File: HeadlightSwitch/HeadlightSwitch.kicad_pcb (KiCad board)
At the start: 2 copper layers, 88.4 x 25.4 mm, 24 parts, among them J0 Battery-, J101 Battery+, J102 MarkerTail+, J103 Headlight+, J104 Headlight-, Q101 BCX56, SW101 SW_Rotary3x4, U101 LM555xM

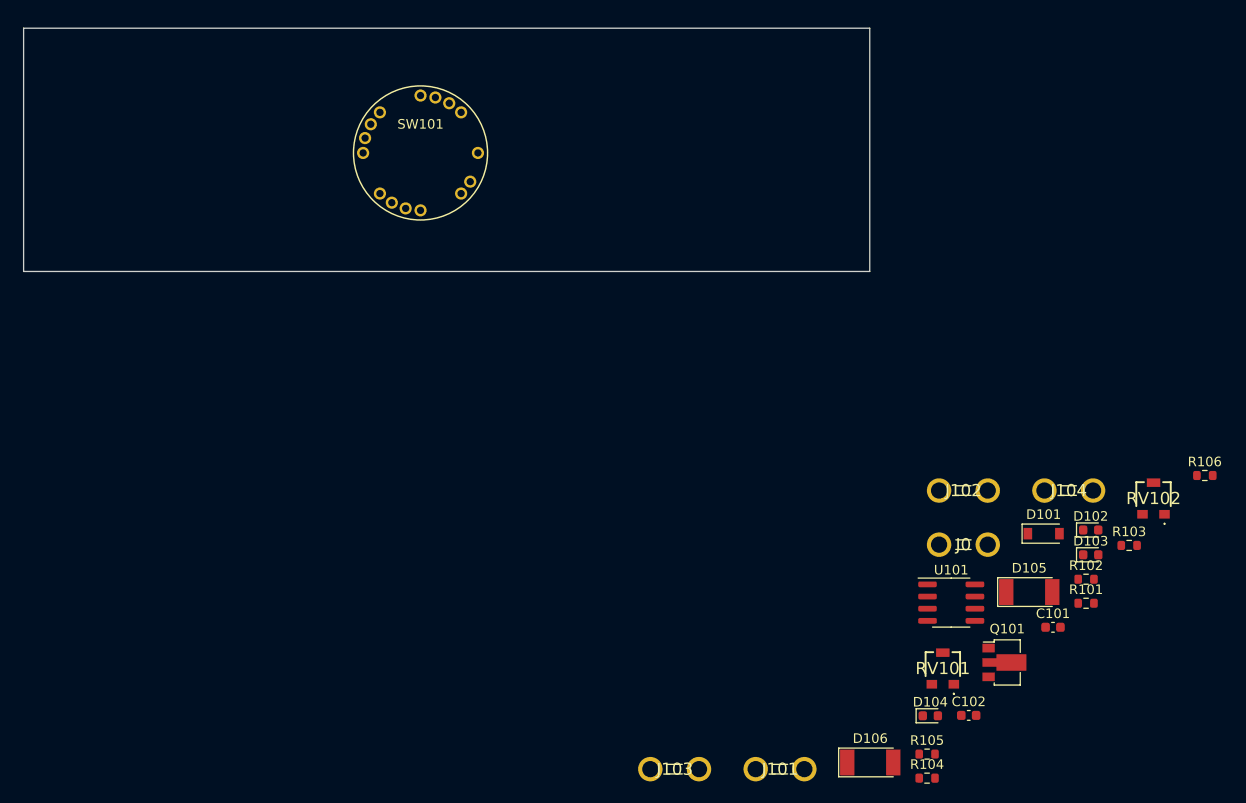
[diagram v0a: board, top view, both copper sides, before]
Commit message: Complete Headlight Switch Board.
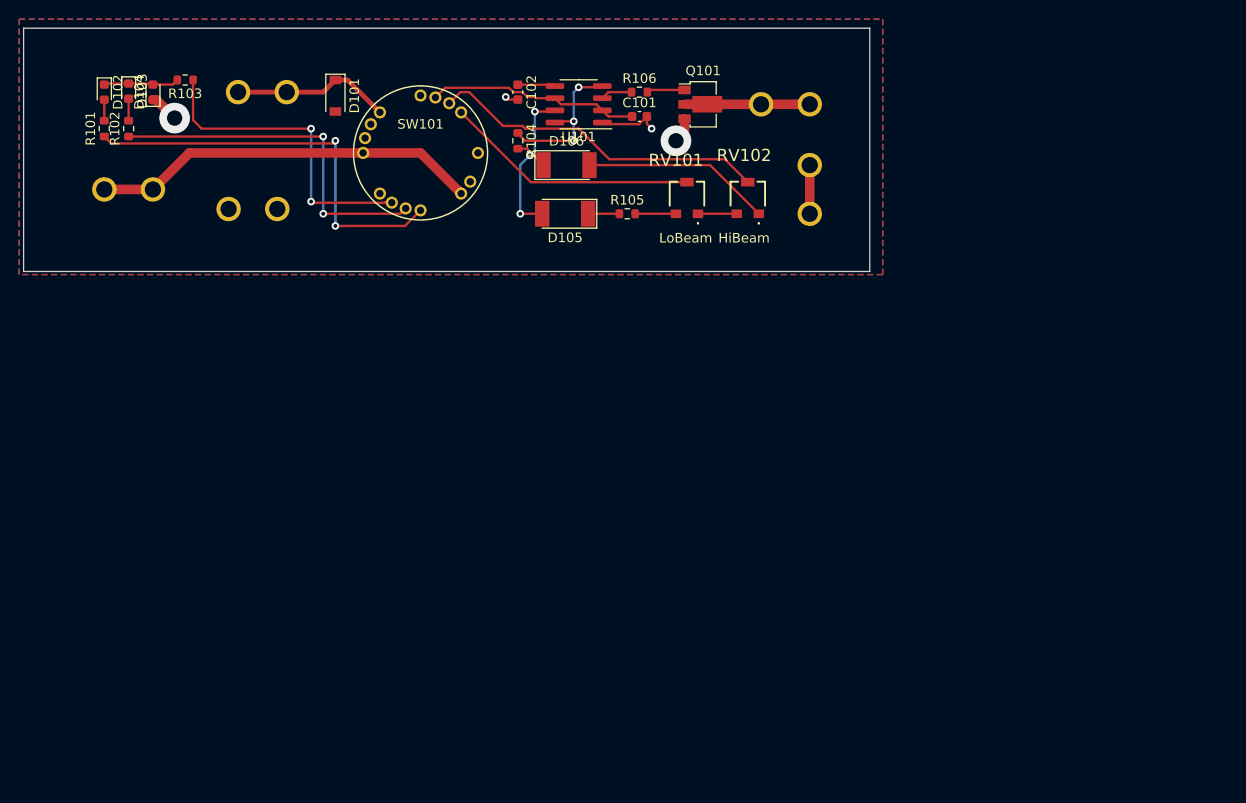
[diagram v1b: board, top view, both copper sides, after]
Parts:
- J0, J101, J102, J103, J104: moved to B.Cu
- moved R101 113.9 mm to (95.2, 67.3), turned to 90 degrees
- moved D102 112.7 mm to (95.2, 63.5), turned to -90 degrees
- moved D103 111.5 mm to (97.8, 63.4), turned to -90 degrees
- moved R102 110.5 mm to (97.8, 67.3), turned to 90 degrees
- moved R103 109.9 mm to (103.7, 62.2), turned to 180 degrees
- moved D104 104.1 mm to (100.3, 63.5), turned to 90 degrees
- moved J101 91.0 mm to (95.2, 73.7)
- moved D101 86.9 mm to (119.4, 63.9), turned to -90 degrees
- moved C102 80.3 mm to (138.4, 63.5), turned to -90 degrees
- moved J102 79.8 mm to (114.3, 63.5), turned to 180 degrees
- moved R104 79.1 mm to (138.4, 68.6), turned to -90 degrees
- moved J0 77.5 mm to (113.3, 75.7), turned to 180 degrees
- moved R106 71.3 mm to (151.1, 63.5)
- moved D106 70.0 mm to (143.5, 71.1)
- moved C101 68.6 mm to (151.1, 66.0)
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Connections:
- net Net-(D101-Pad1) renamed /MarkerTail+
- net Net-(J104-Pad1) renamed /Headlight-
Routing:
- net Net-(R101-Pad1): track 0.00 -> 43.0 mm, vias 0 -> 2
- net +12V: track 0.00 -> 40.6 mm
- net Net-(R102-Pad1): track 0.00 -> 37.2 mm, vias 0 -> 2
- net /PWHigh: track 0.00 -> 35.5 mm
- net Net-(R103-Pad1): track 0.00 -> 33.0 mm, vias 0 -> 2
- net /PWLow: track 0.00 -> 26.6 mm
- net /PWCommon: track 0.00 -> 22.2 mm
- net /HLightPower: track 0.00 -> 22.1 mm, vias 0 -> 3
- net Net-(D105-Pad2): track 0.00 -> 21.3 mm, vias 0 -> 3
- net Net-(D106-Pad2): track 0.00 -> 19.8 mm
- net /MarkerTail+: track 0.00 -> 16.7 mm
- net GNDPWR: track 0.00 -> 13.6 mm, vias 0 -> 4
- net /Headlight-: track 0.00 -> 13.0 mm
- net Net-(D102-Pad1): track 0.00 -> 7.91 mm
- net Net-(R105-Pad2): track 0.00 -> 4.25 mm
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- added copper zone on F.Cu, net /HLightPower
- added copper zone on B.Cu, net GNDPWR
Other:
- board text added: "HiBeam"
- board text added: "LoBeam"

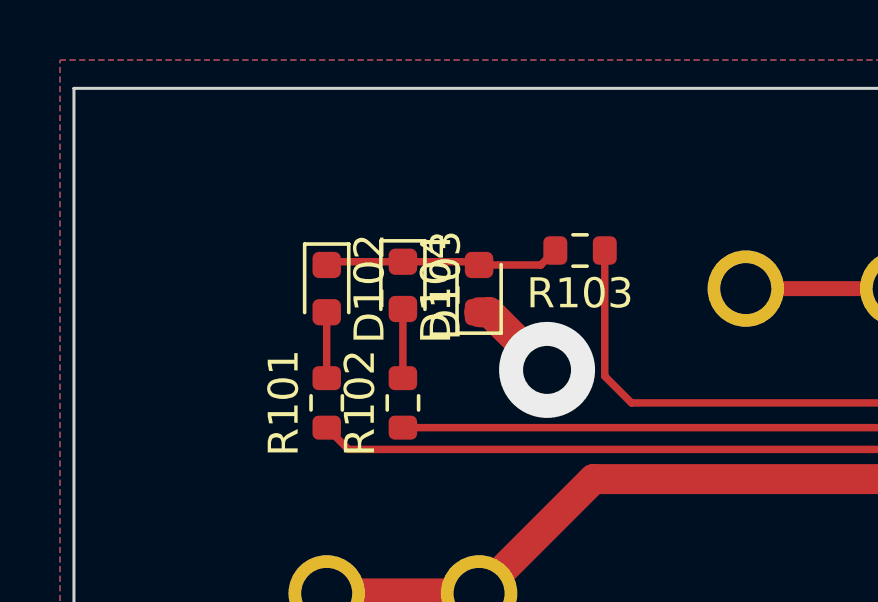
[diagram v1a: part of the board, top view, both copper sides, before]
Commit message: Add dims.
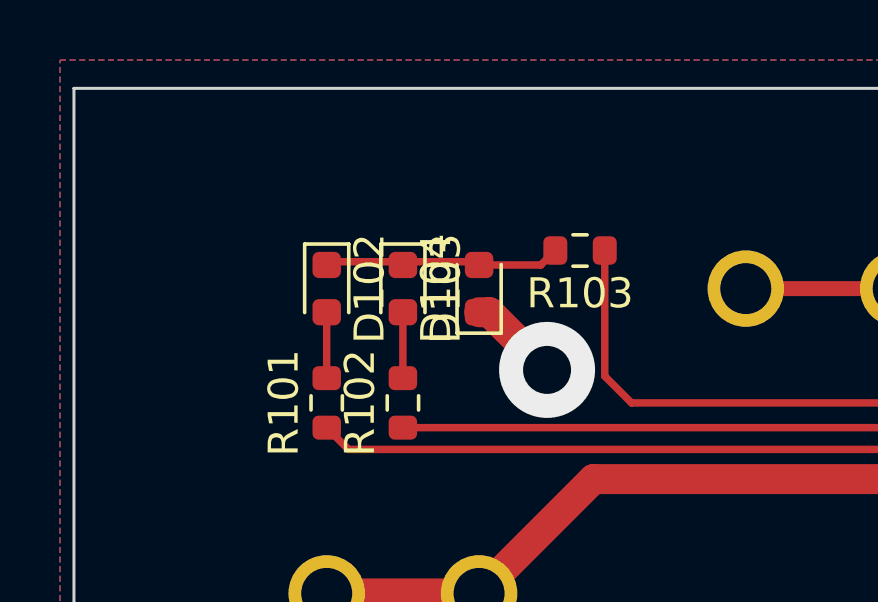
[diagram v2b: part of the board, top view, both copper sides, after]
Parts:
- moved D103 0.11 mm to (97.8, 63.5)
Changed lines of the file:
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@@
   )
   (footprint "LED_SMD:LED_0603_1608Metric" (layer "F.Cu")
-    (at 97.79 63.3925 -90)
+    (at 97.79 63.5 -90)
     (descr "LED SMD 0603 (1608 Metric), square (rectangular) end terminal, IPC_7351 nominal, (Body size source: http://www.tortai-tech.com/upload/download/2011102023233369053.pdf), generated with kicad-footprint-generator")
     (tags "LED")
@@
     )
   )
+  (gr_line (start 100.33 63.5) (end 86.868 63.5) (layer "Dwgs.User") (width 0.15))
   (gr_rect (start 90 60) (end 172 79.05) (layer "Dwgs.User") (width 0.2) (fill none))
   (gr_rect (start 86.825 56.825) (end 175.175 82.225) (layer "Edge.Cuts") (width 0.1) (fill none))
@@
     (effects (font (size 1 1) (thickness 0.15)))
   )
+  (dimension (type aligned) (layer "Dwgs.User")
+    (pts (xy 175.175 82.225) (xy 175.175 56.825))
+    (height 11.261)
+    (gr_text "25.4000 mm" (at 185.286 69.525 90) (layer "Dwgs.User")
+      (effects (font (size 1 1) (thickness 0.15)))
+    )
+    (format (units 3) (units_format 1) (precision 4))
+    (style (thickness 0.15) (arrow_length 1.27) (text_position_mode 0) (extension_height 0.58642) (extension_offset 0.5) keep_text_aligned)
+  )
+  (dimension (type aligned) (layer "Dwgs.User")
+    (pts (xy 172 60) (xy 90 60))
+    (height 7.93)
+    (gr_text "82.0000 mm" (at 131 50.92) (layer "Dwgs.User")
+      (effects (font (size 1 1) (thickness 0.15)))
+    )
+    (format (units 3) (units_format 1) (precision 4))
+    (style (thickness 0.15) (arrow_length 1.27) (text_position_mode 0) (extension_height 0.58642) (extension_offset 0.5) keep_text_aligned)
+  )
+  (dimension (type aligned) (layer "Dwgs.User")
+    (pts (xy 95.25 63.5) (xy 95.25 56.896))
+    (height -10.414)
+    (gr_text "6.6040 mm" (at 83.686 60.198 90) (layer "Dwgs.User")
+      (effects (font (size 1 1) (thickness 0.15)))
+    )
+    (format (units 3) (units_format 1) (precision 4))
+    (style (thickness 0.15) (arrow_length 1.27) (text_position_mode 0) (extension_height 0.58642) (extension_offset 0.5) keep_text_aligned)
+  )
+  (dimension (type aligned) (layer "Dwgs.User")
+    (pts (xy 97.79 63.5) (xy 95.25 63.5))
+    (height 13.208)
+    (gr_text "2.5400 mm" (at 96.52 49.142) (layer "Dwgs.User")
+      (effects (font (size 1 1) (thickness 0.15)))
+    )
+    (format (units 3) (units_format 1) (precision 4))
+    (style (thickness 0.15) (arrow_length 1.27) (text_position_mode 0) (extension_height 0.58642) (extension_offset 0.5) keep_text_aligned)
+  )
+  (dimension (type aligned) (layer "Dwgs.User")
+    (pts (xy 100.33 63.5) (xy 97.79 63.5))
+    (height 15.747999)
+    (gr_text "2.5400 mm" (at 99.06 46.602001) (layer "Dwgs.User")
+      (effects (font (size 1 1) (thickness 0.15)))
+    )
+    (format (units 3) (units_format 1) (precision 4))
+    (style (thickness 0.15) (arrow_length 1.27) (text_position_mode 0) (extension_height 0.58642) (extension_offset 0.5) keep_text_aligned)
+  )
+  (dimension (type aligned) (layer "Dwgs.User")
+    (pts (xy 86.825 56.825) (xy 175.175 56.825))
+    (height -13.391)
+    (gr_text "88.3500 mm" (at 131 42.284) (layer "Dwgs.User")
+      (effects (font (size 1 1) (thickness 0.15)))
+    )
+    (format (units 3) (units_format 1) (precision 4))
+    (style (thickness 0.15) (arrow_length 1.27) (text_position_mode 0) (extension_height 0.58642) (extension_offset 0.5) keep_text_aligned)
+  )
+  (dimension (type aligned) (layer "Dwgs.User")
+    (pts (xy 95.25 63.5) (xy 86.868 63.5))
+    (height 8.635999)
+    (gr_text "8.3820 mm" (at 91.059 53.714001) (layer "Dwgs.User")
+      (effects (font (size 1 1) (thickness 0.15)))
+    )
+    (format (units 3) (units_format 1) (precision 4))
+    (style (thickness 0.15) (arrow_length 1.27) (text_position_mode 0) (extension_height 0.58642) (extension_offset 0.5) keep_text_aligned)
+  )
+  (dimension (type aligned) (layer "Dwgs.User")
+    (pts (xy 128.27 69.85) (xy 86.825 69.85))
+    (height -15.748)
+    (gr_text "41.4450 mm" (at 107.5475 84.448) (layer "Dwgs.User")
+      (effects (font (size 1 1) (thickness 0.15)))
+    )
+    (format (units 3) (units_format 1) (precision 4))
+    (style (thickness 0.15) (arrow_length 1.27) (text_position_mode 0) (extension_height 0.58642) (extension_offset 0.5) keep_text_aligned)
+  )
+  (dimension (type aligned) (layer "Dwgs.User")
+    (pts (xy 172 60) (xy 172 79.05))
+    (height -8.34)
+    (gr_text "19.0500 mm" (at 179.19 69.525 90) (layer "Dwgs.User")
+      (effects (font (size 1 1) (thickness 0.15)))
+    )
+    (format (units 3) (units_format 1) (precision 4))
+    (style (thickness 0.15) (arrow_length 1.27) (text_position_mode 0) (extension_height 0.58642) (extension_offset 0.5) keep_text_aligned)
+  )
+  (dimension (type aligned) (layer "Dwgs.User")
+    (pts (xy 128.27 69.85) (xy 128.27 56.896))
+    (height -45.974)
+    (gr_text "12.9540 mm" (at 81.146 63.373 90) (layer "Dwgs.User")
+      (effects (font (size 1 1) (thickness 0.15)))
+    )
+    (format (units 3) (units_format 1) (precision 4))
+    (style (thickness 0.15) (arrow_length 1.27) (text_position_mode 0) (extension_height 0.58642) (extension_offset 0.5) keep_text_aligned)
+  )
   (segment (start 139.415817 64.008) (end 138.907817 63.5) (width 0.25) (layer "F.Cu") (net 1))

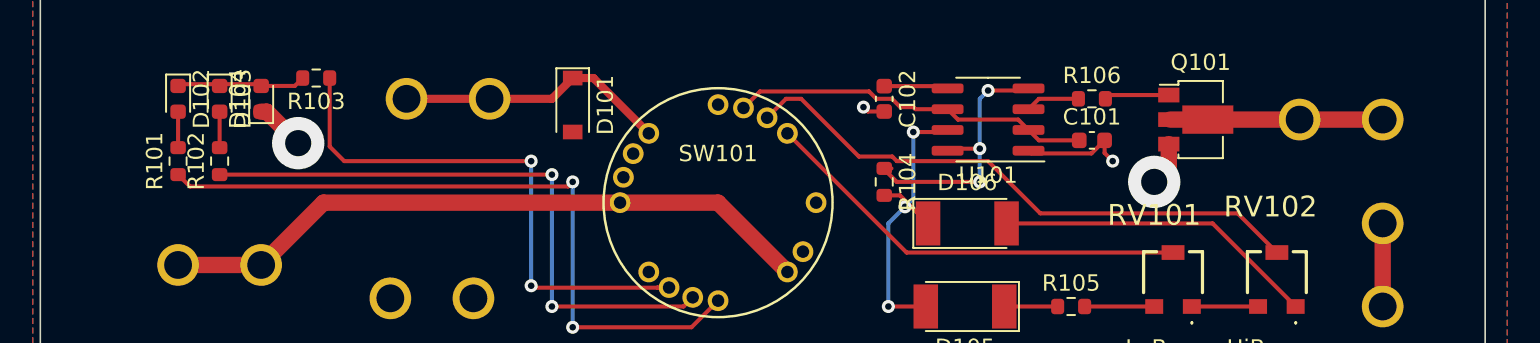
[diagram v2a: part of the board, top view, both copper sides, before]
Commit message: Add Mounting Holes with dims.
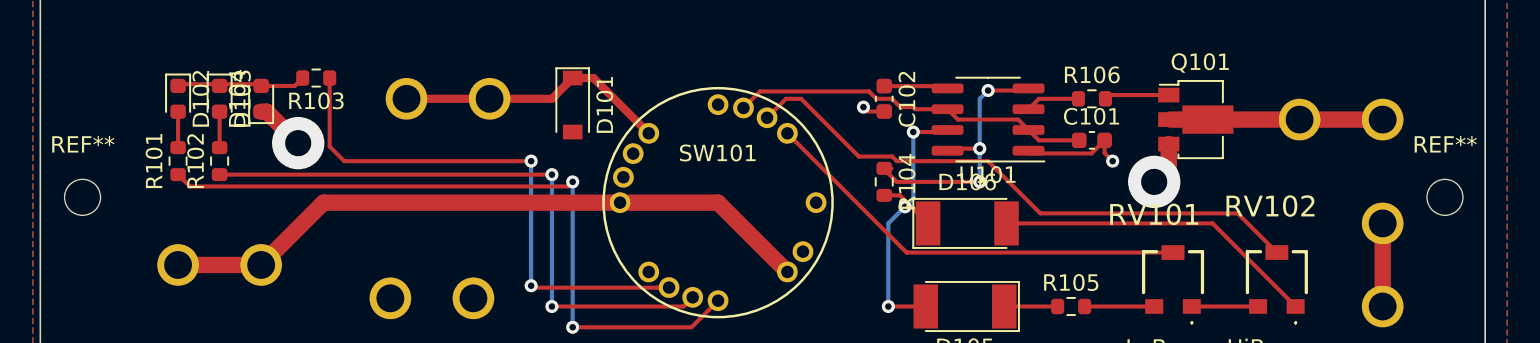
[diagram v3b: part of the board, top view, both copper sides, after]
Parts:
- added REF**: MountingHole_2.2mm_M2, MountingHole:MountingHole_2.2mm_M2, F.Cu at (89.4, 69.5)
- added REF**: MountingHole_2.2mm_M2, MountingHole:MountingHole_2.2mm_M2, F.Cu at (172.7, 69.5)
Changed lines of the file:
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@@
     )
+  )
+  (footprint "MountingHole:MountingHole_2.2mm_M2" (layer "F.Cu")
+    (at 89.408 69.525)
+    (descr "Mounting Hole 2.2mm, no annular, M2")
+    (tags "mounting hole 2.2mm no annular m2")
+    (attr exclude_from_pos_files exclude_from_bom)
+    (fp_text reference "REF**" (at 0 -3.2) (layer "F.SilkS")
+      (effects (font (size 1 1) (thickness 0.15)))
+    )
+    (fp_text value "MountingHole_2.2mm_M2" (at 0 3.2) (layer "F.Fab")
+      (effects (font (size 1 1) (thickness 0.15)))
+    )
+    (fp_text user "${REFERENCE}" (at 0 0) (layer "F.Fab")
+      (effects (font (size 1 1) (thickness 0.15)))
+    )
+    (fp_circle (center 0 0) (end 2.2 0) (layer "Cmts.User") (width 0.15) (fill none))
+    (fp_circle (center 0 0) (end 2.45 0) (layer "F.CrtYd") (width 0.05) (fill none))
+    (pad "" np_thru_hole circle (at 0 0) (size 2.2 2.2) (drill 2.2) (layers *.Cu *.Mask))
   )
   (footprint "BournsPVG3A:PVG3A103C01R00" (layer "F.Cu")
@@
     )
   )
+  (footprint "MountingHole:MountingHole_2.2mm_M2" (layer "F.Cu")
+    (at 172.72 69.525)
+    (descr "Mounting Hole 2.2mm, no annular, M2")
+    (tags "mounting hole 2.2mm no annular m2")
+    (attr exclude_from_pos_files exclude_from_bom)
+    (fp_text reference "REF**" (at 0 -3.2) (layer "F.SilkS")
+      (effects (font (size 1 1) (thickness 0.15)))
+    )
+    (fp_text value "MountingHole_2.2mm_M2" (at 0 3.2) (layer "F.Fab")
+      (effects (font (size 1 1) (thickness 0.15)))
+    )
+    (fp_text user "${REFERENCE}" (at 0 0) (layer "F.Fab")
+      (effects (font (size 1 1) (thickness 0.15)))
+    )
+    (fp_circle (center 0 0) (end 2.2 0) (layer "Cmts.User") (width 0.15) (fill none))
+    (fp_circle (center 0 0) (end 2.45 0) (layer "F.CrtYd") (width 0.05) (fill none))
+    (pad "" np_thru_hole circle (at 0 0) (size 2.2 2.2) (drill 2.2) (layers *.Cu *.Mask))
+  )
   (footprint "Diode_SMD:D_SOD-123" (layer "F.Cu")
     (at 119.38 63.88 -90)
@@
   )
   (dimension (type aligned) (layer "Dwgs.User")
+    (pts (xy 90.17 69.525) (xy 90.17 82.2706))
+    (height 6.2484)
+    (gr_text "12.7 mm" (at 82.7716 75.8978 90) (layer "Dwgs.User")
+      (effects (font (size 1 1) (thickness 0.15)))
+    )
+    (format (units 3) (units_format 1) (precision 4) (override_value "12.7"))
+    (style (thickness 0.15) (arrow_length 1.27) (text_position_mode 0) (extension_height 0.58642) (extension_offset 0.5) keep_text_aligned)
+  )
+  (dimension (type aligned) (layer "Dwgs.User")
     (pts (xy 172 60) (xy 90 60))
     (height 7.93)
@@
   )
   (dimension (type aligned) (layer "Dwgs.User")
+    (pts (xy 172.72 69.525) (xy 175.17 69.525))
+    (height 16.835)
+    (gr_text "2.4500 mm" (at 173.945 85.21) (layer "Dwgs.User")
+      (effects (font (size 1 1) (thickness 0.15)))
+    )
+    (format (units 3) (units_format 1) (precision 4))
+    (style (thickness 0.15) (arrow_length 1.27) (text_position_mode 0) (extension_height 0.58642) (extension_offset 0.5) keep_text_aligned)
+  )
+  (dimension (type aligned) (layer "Dwgs.User")
     (pts (xy 86.825 56.825) (xy 175.175 56.825))
     (height -13.391)
@@
       (effects (font (size 1 1) (thickness 0.15)))
     )
+    (format (units 3) (units_format 1) (precision 4))
+    (style (thickness 0.15) (arrow_length 1.27) (text_position_mode 0) (extension_height 0.58642) (extension_offset 0.5) keep_text_aligned)
+  )
+  (dimension (type aligned) (layer "Dwgs.User")
+    (pts (xy 89.408 69.525) (xy 86.958 69.525))
+    (height -20.137)
+    (gr_text "2.4500 mm" (at 88.183 88.512) (layer "Dwgs.User")
+      (effects (font (size 1 1) (thickness 0.15)))
+    )
